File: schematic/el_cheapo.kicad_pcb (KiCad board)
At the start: 2 copper layers, 100.7 x 80.4 mm, 57 parts, among them J1 Conn_01x02, J2 Conn_01x02, J3 Conn_01x02, Q1 TIP32A, Q2 2N3904, Q3 2N3906, Q4 2N3904, Q5 TIP31A, Q6 TIP32A, Q7 2N3055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

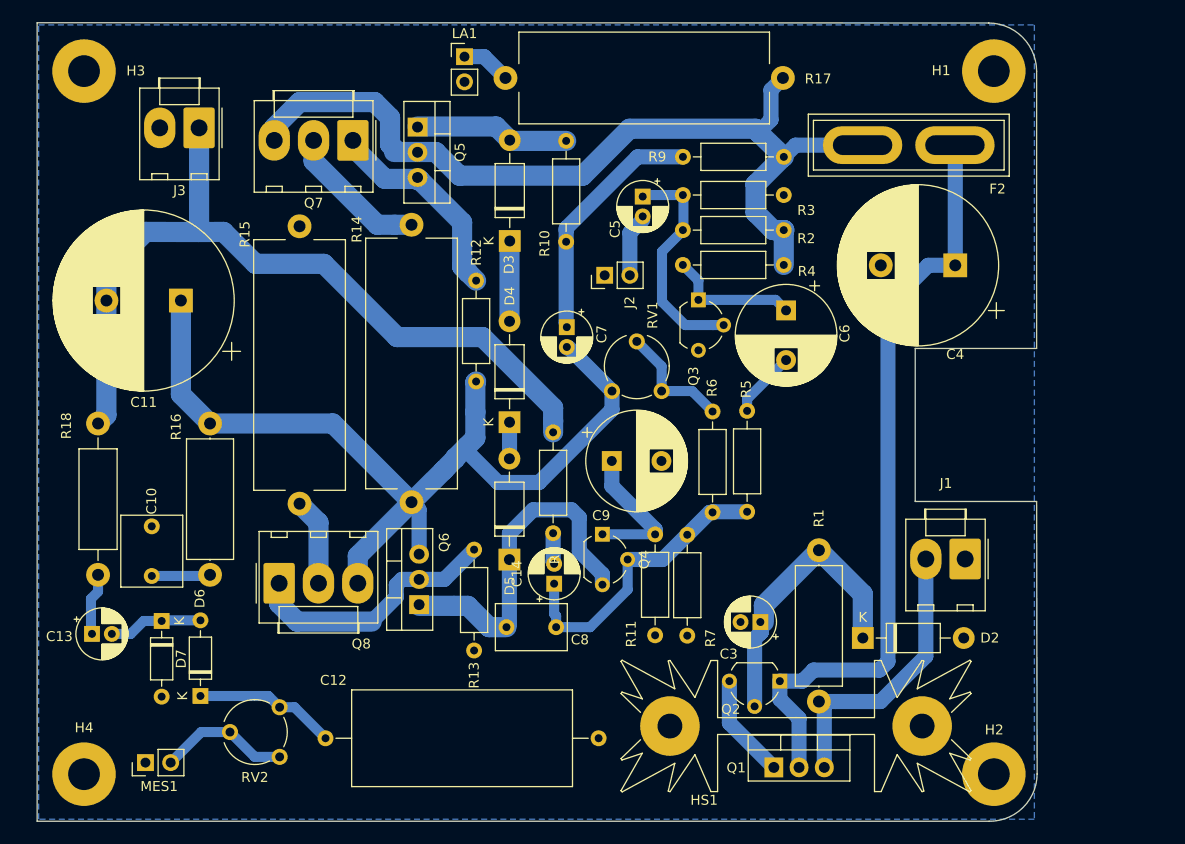
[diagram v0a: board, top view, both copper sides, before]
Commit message: altered boards to fit dynaco amps of a similar design.
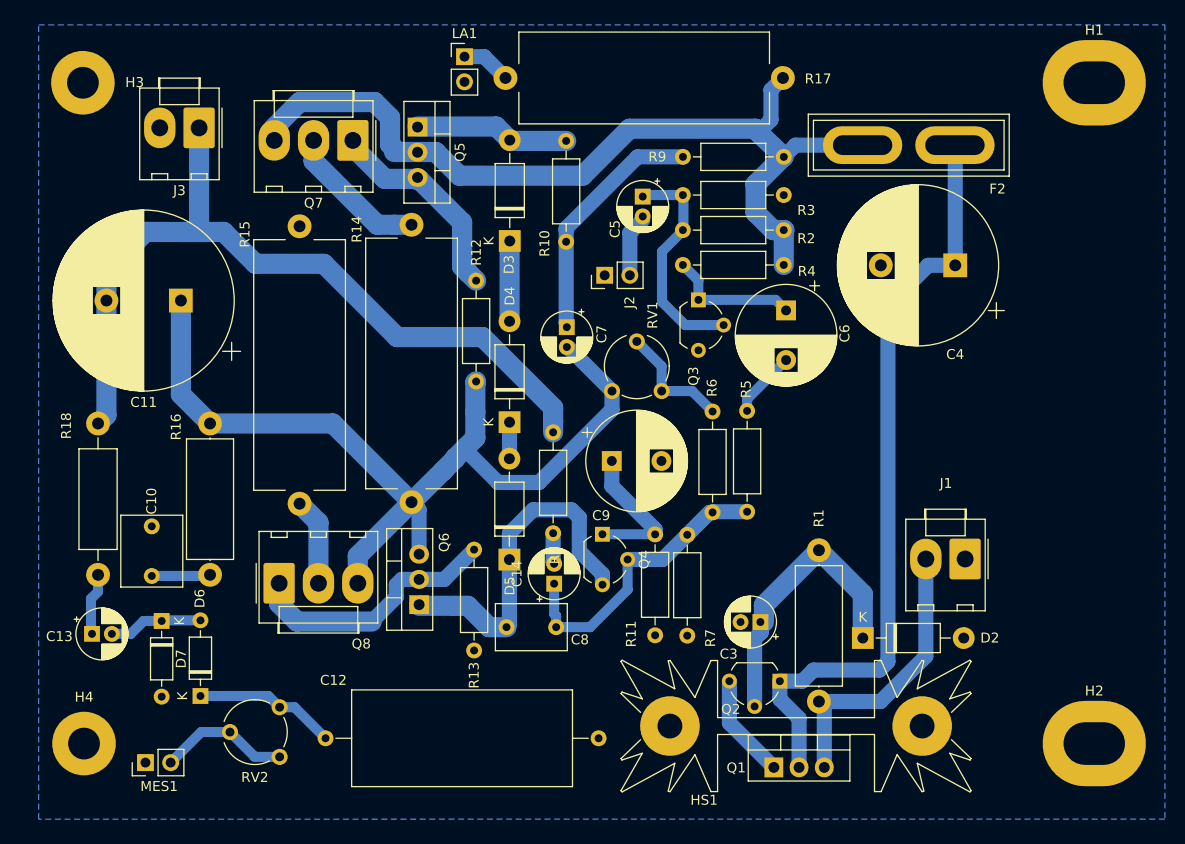
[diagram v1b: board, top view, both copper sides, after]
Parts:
- C12: value 0.1uF -> 0.47uF
- D2: value 33 -> 39
- F2: value 1A -> 2A
- H1, H2: footprint MountingHole:MountingHole_3.2mm_M3_Pad -> MountingHole:MountingHole_4.3x6.2mm_M4_Pad
- R18: value 1k_100k 1W -> 10k 1W
- RV1: value 120k -> 220k
- RV2: value 1k_100K -> 47K
- moved H2 10.6 mm to (194.1, 130.7)
- moved H1 10.2 mm to (194.1, 64.1)
- moved H4 3.08 mm to (92.3, 130.7)
- moved H3 1.18 mm to (92.2, 64.1)
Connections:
- H1 pad 1: GND -> Net-(H1-Pad1)
- H2 pad 1: GND -> Net-(H2-Pad1)
- H3 pad 1: GND -> Net-(H3-Pad1)
- H4 pad 1: GND -> Net-(H4-Pad1)
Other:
- board outline removed

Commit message: updated dynaco footprint. First try wasn't perfect. This offers some flexability by using oblong holes.
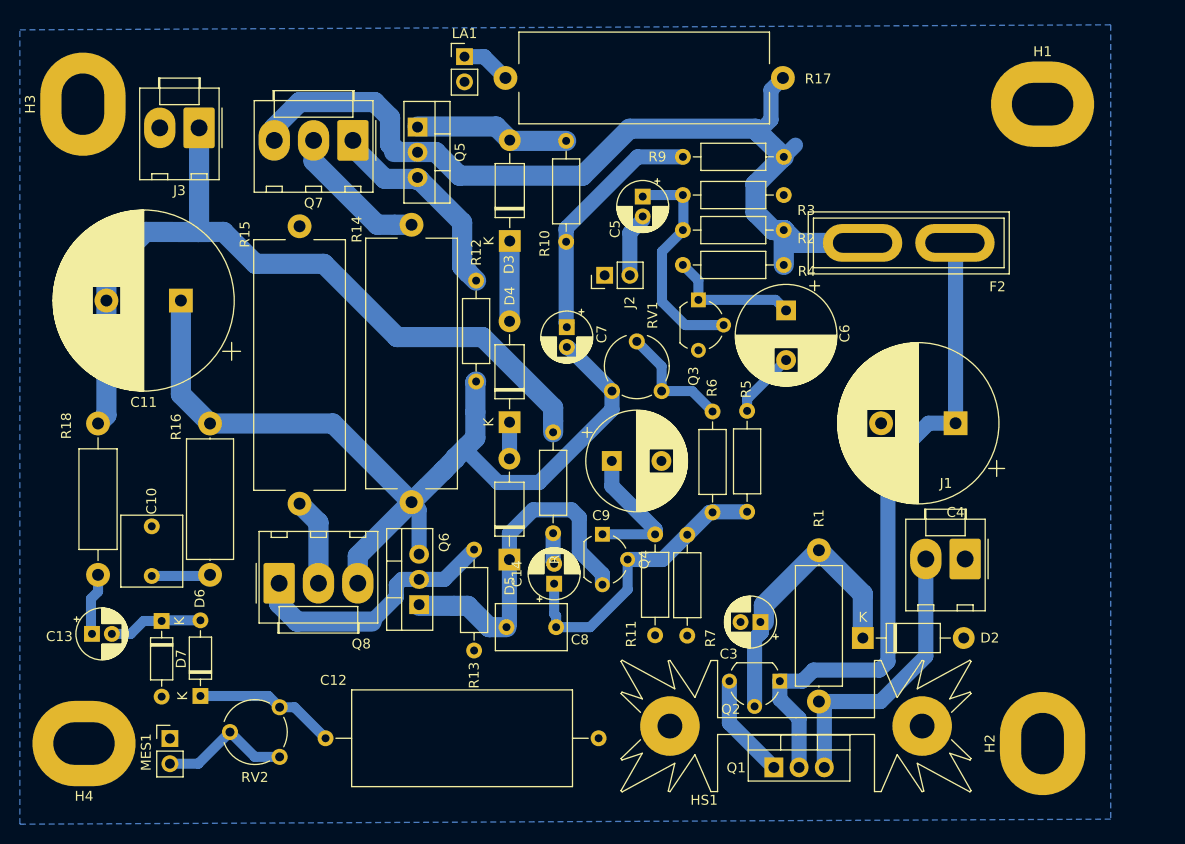
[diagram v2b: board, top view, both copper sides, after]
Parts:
- H3, H4: footprint MountingHole:MountingHole_3.2mm_M3_Pad -> MountingHole:MountingHole_4.3x6.2mm_M4_Pad
- moved C4 15.9 mm to (180.1, 98.4)
- moved F2 9.85 mm to (170.7, 80.3)
- moved H1 5.64 mm to (188.8, 66.3)
- moved H2 5.21 mm to (188.8, 130.7), turned to 90 degrees
- moved MES1 3.46 mm to (101.0, 130.2), turned to 0 degrees
- moved H3 2.16 mm to (92.2, 66.3), turned to 90 degrees
- turned H4 to 180 degrees
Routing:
- net Net-(C4-Pad1): track 77.6 -> 67.8 mm
- net /amp/+V: track 90.4 -> 92.1 mm
